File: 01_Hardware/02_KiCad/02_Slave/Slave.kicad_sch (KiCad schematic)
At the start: 12 parts, among them J1 Screw_Terminal_01x04, J2 Conn_01x30_Female, J3 Screw_Terminal_01x04, J4 Conn_01x30_Female, Q1 AO3400A, Q2 AO3400A, U1 LM393

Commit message: KiCAD
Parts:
- removed J2, J4: Conn_01x30_Female, Connector_PinSocket_2.54mm:PinSocket_1x30_P2.54mm_Vertical, symbol Connector:Conn_01x30_Female
- removed R1: 1k, Resistor_THT:R_Axial_DIN0204_L3.6mm_D1.6mm_P5.08mm_Horizontal, symbol Device:R
- added J1, J2: Conn_01x22_Female, symbol Connector:Conn_01x22_Female
- added R4, R9: 10k, symbol Device:R
- added R8: 14.3k, symbol Device:R
- R2: value 4k -> 10k; footprint Resistor_THT:R_Axial_DIN0204_L3.6mm_D1.6mm_P5.08mm_Horizontal -> (none)
- R3: footprint Resistor_THT:R_Axial_DIN0204_L3.6mm_D1.6mm_P5.08mm_Horizontal -> (none)
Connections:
- net Bus: now also R2.1; no longer U1.3 (+)
- net GND: now also R3.2, J1.GND (Pin_22), R8.2; no longer R2.2
- net at Q1.1 (G): now also J1.GPIO17 (Pin_10)
- net at Q2.1 (G): now also J1.GPIO18 (Pin_11)
- net at U1.2 (-): now also R8.1, R9.2; no longer R2.1
- net at U1.1: now also R4.1; no longer R3.2
- net at R3.1: now also R2.2, U1.3 (+)
- new net 3.3V: R4.2, R9.1

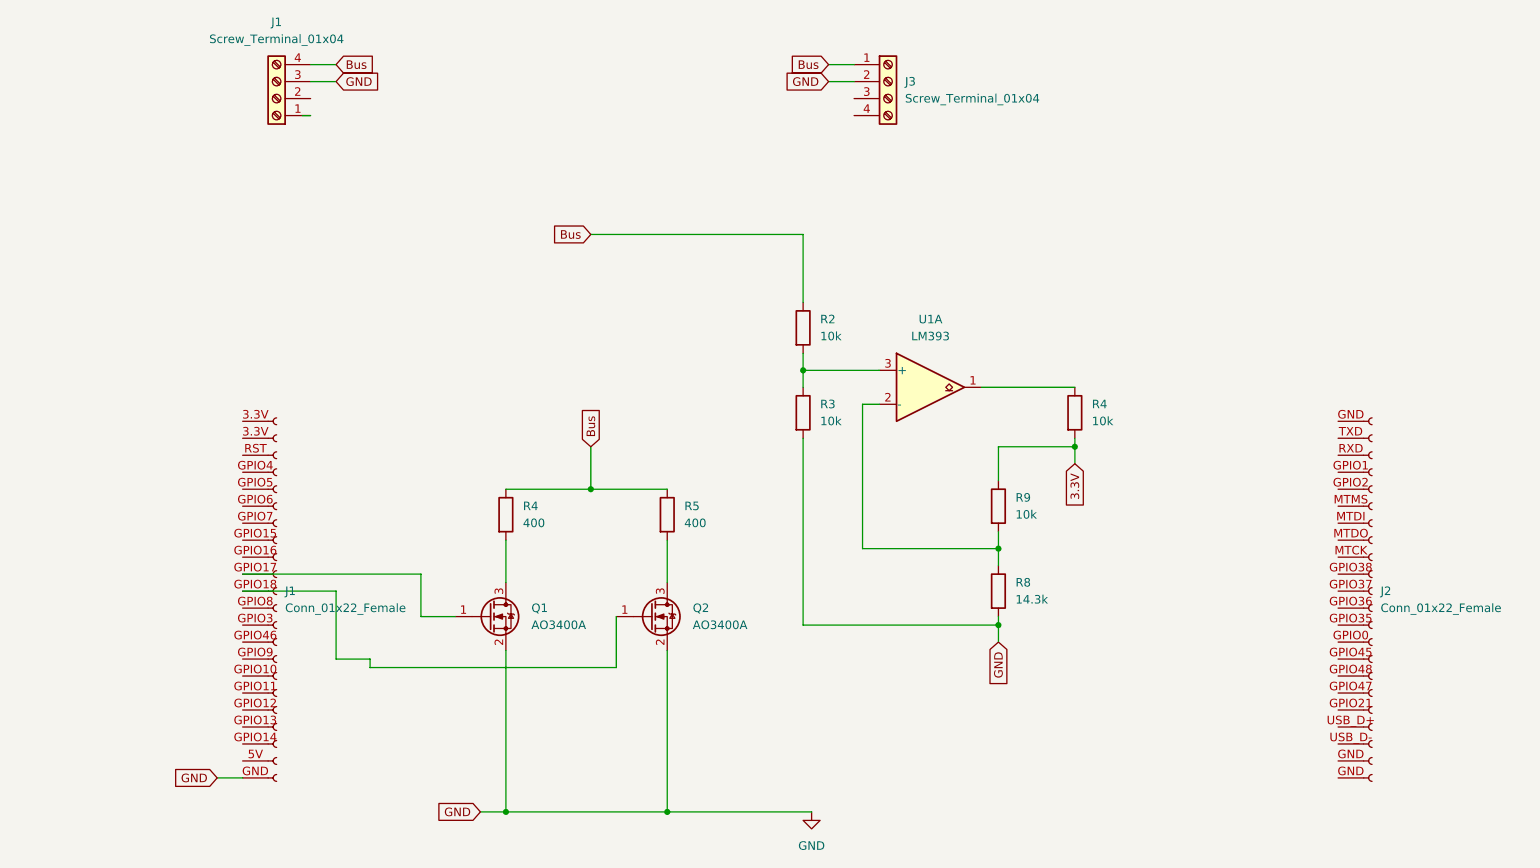
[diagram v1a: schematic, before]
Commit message: KiCad Slave Update, now routed
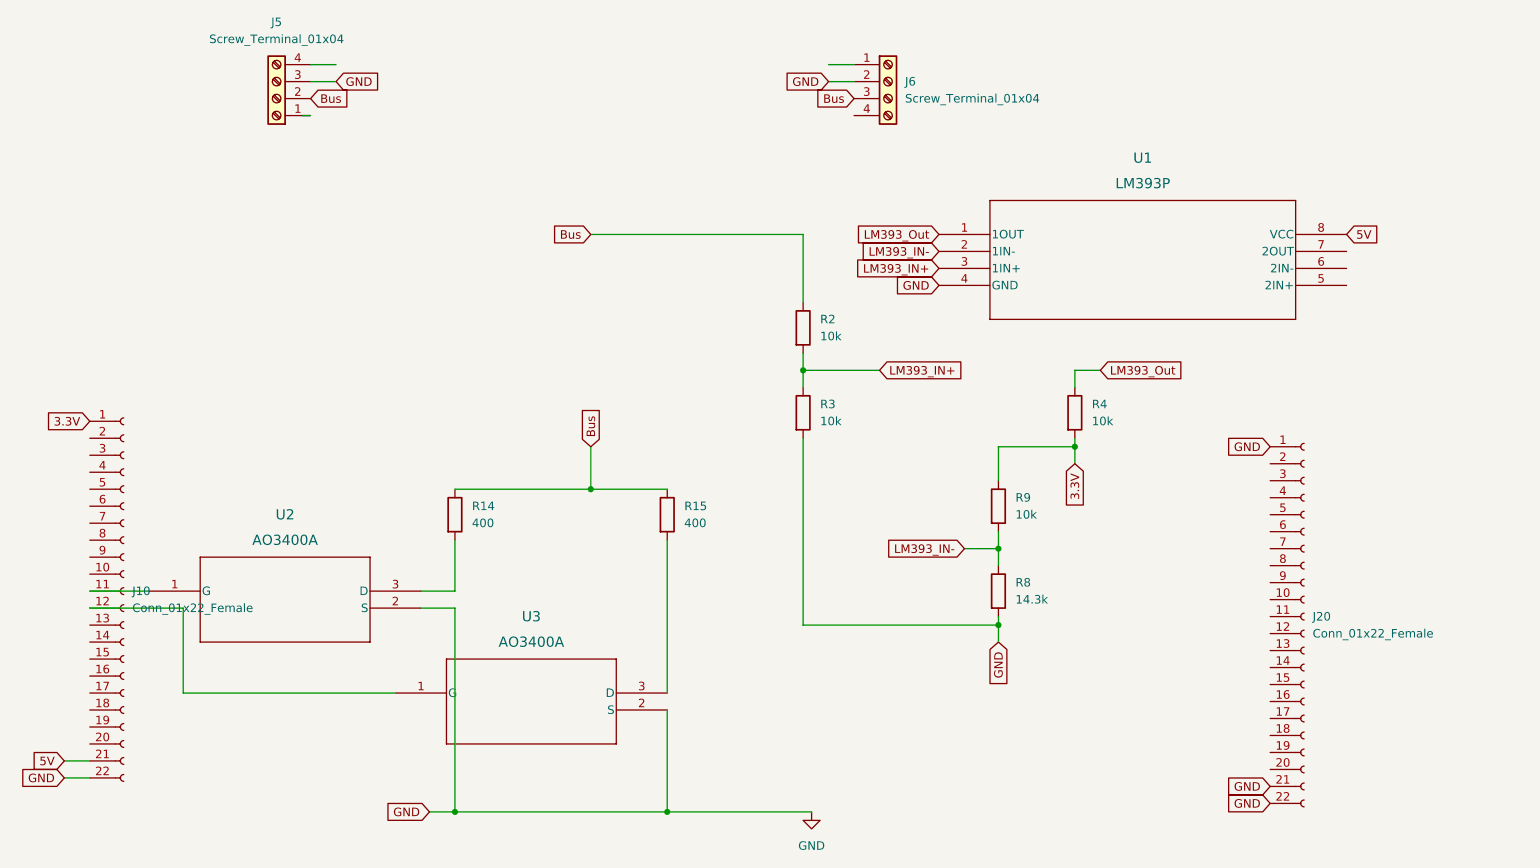
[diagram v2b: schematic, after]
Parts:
- removed J1, J2: Conn_01x22_Female, symbol Connector:Conn_01x22_Female
- removed Q1, Q2: AO3400A, Package_TO_SOT_SMD:SOT-23, symbol Transistor_FET:AO3400A
- removed U1: LM393, Package_DIP:DIP-4_W7.62mm, symbol Comparator:LM393
- added J10, J20: Conn_01x22_Female, Connector_PinSocket_2.54mm:PinSocket_1x22_P2.54mm_Vertical, symbol Connector:Conn_01x22_Female
- added U1: LM393P, LM393:P8, symbol LM393:LM393P
- added U2, U3: AO3400A, AO3400A:SOT-23-3L_AOS, symbol AO3400A:AO3400A
- R2, R3, R4, R8, R9: footprint (none) -> Resistor_THT:R_Axial_DIN0204_L3.6mm_D1.6mm_P5.08mm_Horizontal
- renumbered J1 to J5, J3 to J6, R4 to R14, R5 to R15
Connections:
- net 3.3V: now also J10.1 (Pin_1)
- net Bus: now also J5.2 (Pin_2), J6.3 (Pin_3); no longer J5.4 (Pin_4), J6.1 (Pin_1)
- net GND: now also J10.22 (Pin_22), J20.1 (Pin_1), J20.21 (Pin_21), J20.22 (Pin_22), U1.4 (GND), U2.2 (S), U3.2 (S)
- net at R14.2: now also U2.3 (D)
- net LM393_Out: now reaches R4.1
- net LM393_Out: now also U1.1 (1OUT)
- net LM393_IN+: now reaches R2.2, R3.1
- net LM393_IN+: now also U1.3 (1IN+)
- net LM393_IN-: now reaches R8.1, R9.2
- net LM393_IN-: now also U1.2 (1IN-)
- net at R15.2: now also U3.3 (D)
- new net: J10.11 (Pin_11), U2.1 (G)
- new net: J10.12 (Pin_12), U3.1 (G)
- new net 5V: J10.21 (Pin_21), U1.8 (VCC)
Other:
- moved on the sheet: R14
